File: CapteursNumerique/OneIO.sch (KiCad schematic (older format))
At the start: 5 parts, among them J14 Conn IO, J15 DIS LED

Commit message: Capteurs num production
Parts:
- D8: LCSC Part (none) -> C74346
- J14: JLCPCB BOM (none) -> 0
- J15: footprint Jumper:SolderJumper-2_P1.3mm_Bridged2Bar_Pad1.0x1.5mm -> Jumper:SolderJumper-2_P1.3mm_Open_Pad1.0x1.5mm; JLCPCB BOM (none) -> 0
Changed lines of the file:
@@
 $Descr A4 11693 8268
 encoding utf-8
-Sheet 4 9
+Sheet 9 9
 Title ""
 Date ""
@@
 AR Path="/5FC99C55/5FC6EE3F" Ref="#PWR010"  Part="1"
 AR Path="/5FC9F45B/5FC6EE3F" Ref="#PWR016"  Part="1"
-F 0 "#PWR06" H 5620 3000 50  0001 C CNN
+F 0 "#PWR016" H 5620 3000 50  0001 C CNN
 F 1 "+5V" H 5635 3323 50  0000 C CNN
 F 2 "" H 5620 3150 50  0001 C CNN
@@
 AR Path="/5FC99C55/5FC6F675" Ref="R14"  Part="1"
 AR Path="/5FC9F45B/5FC6F675" Ref="R20"  Part="1"
-F 0 "R10" H 5688 4076 50  0000 L CNN
+F 0 "R20" H 5688 4076 50  0000 L CNN
 F 1 "10k" H 5688 3985 50  0000 L CNN
 F 2 "Resistor_SMD:R_0805_2012Metric_Pad1.20x1.40mm_HandSolder" V 5660 4020 50  0001 C CNN
@@
 AR Path="/5FC99C55/5FC71F08" Ref="R15"  Part="1"
 AR Path="/5FC9F45B/5FC71F08" Ref="R21"  Part="1"
-F 0 "R11" H 6068 4076 50  0000 L CNN
+F 0 "R21" H 6068 4076 50  0000 L CNN
 F 1 "150" H 6068 3985 50  0000 L CNN
 F 2 "Resistor_SMD:R_0805_2012Metric_Pad1.20x1.40mm_HandSolder" V 6040 4020 50  0001 C CNN
@@
 AR Path="/5FC99C55/5FC72465" Ref="D6"  Part="1"
 AR Path="/5FC9F45B/5FC72465" Ref="D9"  Part="1"
-F 0 "D4" V 6039 4242 50  0000 R CNN
+F 0 "D9" V 6039 4242 50  0000 R CNN
 F 1 "YELLOW" V 5948 4242 50  0000 R CNN
 F 2 "LED_SMD:LED_0805_2012Metric_Pad1.15x1.40mm_HandSolder" H 6000 4360 50  0001 C CNN
 F 3 "~" H 6000 4360 50  0001 C CNN
+F 4 "C74346" V 6000 4360 50  0001 C CNN "LCSC Part"
 	1    6000 4360
 	0    -1   -1   0
@@
 AR Path="/5FC99C55/5FC77683" Ref="J11"  Part="1"
 AR Path="/5FC9F45B/5FC77683" Ref="J17"  Part="1"
-F 0 "J7" V 6004 3580 50  0000 L CNN
+F 0 "J17" V 6004 3580 50  0000 L CNN
 F 1 "DIS LED" V 6095 3580 50  0000 L CNN
-F 2 "Jumper:SolderJumper-2_P1.3mm_Bridged2Bar_Pad1.0x1.5mm" H 6000 3500 50  0001 C CNN
+F 2 "Jumper:SolderJumper-2_P1.3mm_Open_Pad1.0x1.5mm" H 6000 3500 50  0001 C CNN
 F 3 "~" H 6000 3500 50  0001 C CNN
+F 4 "0" V 6000 3500 50  0001 C CNN "JLCPCB BOM"
 	1    6000 3500
 	0    1    1    0
@@
 AR Path="/5FC99C55/5FC7B130" Ref="#PWR09"  Part="1"
 AR Path="/5FC9F45B/5FC7B130" Ref="#PWR015"  Part="1"
-F 0 "#PWR05" H 5370 4760 50  0001 C CNN
+F 0 "#PWR015" H 5370 4760 50  0001 C CNN
 F 1 "GND" H 5375 4837 50  0000 C CNN
 F 2 "" H 5370 5010 50  0001 C CNN
@@
 AR Path="/5FC99C55/5FC7CA9C" Ref="J10"  Part="1"
 AR Path="/5FC9F45B/5FC7CA9C" Ref="J16"  Part="1"
-F 0 "J6" H 4938 4505 50  0000 C CNN
+F 0 "J16" H 4938 4505 50  0000 C CNN
 F 1 "Conn IO" H 4938 4596 50  0000 C CNN
 F 2 "Connector_PinHeader_2.54mm:PinHeader_1x03_P2.54mm_Vertical" H 5020 4830 50  0001 C CNN
 F 3 "~" H 5020 4830 50  0001 C CNN
+F 4 "0" H 5020 4830 50  0001 C CNN "JLCPCB BOM"
 	1    5020 4830
 	-1   0    0    1

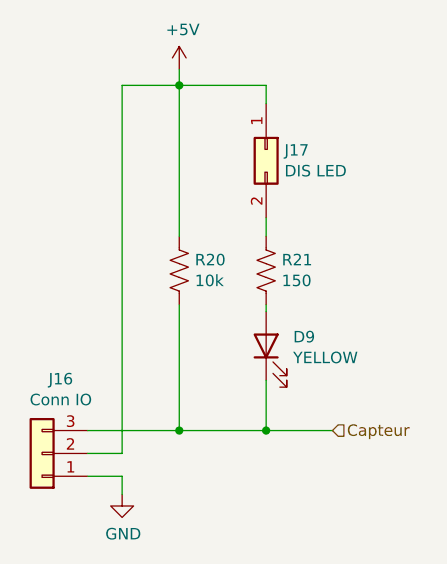
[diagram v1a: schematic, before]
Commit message: Module alim ISO, clean master alim
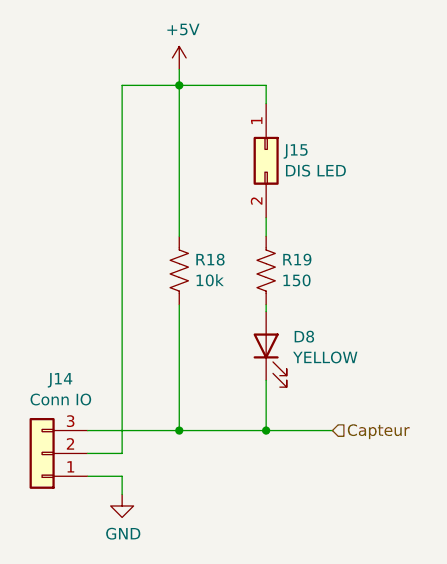
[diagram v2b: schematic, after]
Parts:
- R18: LCSC Part (none) -> C17414
- R19: LCSC Part (none) -> C17471
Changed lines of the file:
@@
 $Descr A4 11693 8268
 encoding utf-8
-Sheet 9 9
+Sheet 8 9
 Title ""
 Date ""
@@
 AR Path="/5FC99C55/5FC6EE3F" Ref="#PWR010"  Part="1"
 AR Path="/5FC9F45B/5FC6EE3F" Ref="#PWR016"  Part="1"
-F 0 "#PWR016" H 5620 3000 50  0001 C CNN
+F 0 "#PWR014" H 5620 3000 50  0001 C CNN
 F 1 "+5V" H 5635 3323 50  0000 C CNN
 F 2 "" H 5620 3150 50  0001 C CNN
@@
 AR Path="/5FC99C55/5FC6F675" Ref="R14"  Part="1"
 AR Path="/5FC9F45B/5FC6F675" Ref="R20"  Part="1"
-F 0 "R20" H 5688 4076 50  0000 L CNN
+F 0 "R18" H 5688 4076 50  0000 L CNN
 F 1 "10k" H 5688 3985 50  0000 L CNN
 F 2 "Resistor_SMD:R_0805_2012Metric_Pad1.20x1.40mm_HandSolder" V 5660 4020 50  0001 C CNN
 F 3 "~" H 5620 4030 50  0001 C CNN
+F 4 "C17414" H 5620 4030 50  0001 C CNN "LCSC Part"
 	1    5620 4030
 	1    0    0    -1
@@
 AR Path="/5FC99C55/5FC71F08" Ref="R15"  Part="1"
 AR Path="/5FC9F45B/5FC71F08" Ref="R21"  Part="1"
-F 0 "R21" H 6068 4076 50  0000 L CNN
+F 0 "R19" H 6068 4076 50  0000 L CNN
 F 1 "150" H 6068 3985 50  0000 L CNN
 F 2 "Resistor_SMD:R_0805_2012Metric_Pad1.20x1.40mm_HandSolder" V 6040 4020 50  0001 C CNN
 F 3 "~" H 6000 4030 50  0001 C CNN
+F 4 "C17471" H 6000 4030 50  0001 C CNN "LCSC Part"
 	1    6000 4030
 	1    0    0    -1
@@
 AR Path="/5FC99C55/5FC72465" Ref="D6"  Part="1"
 AR Path="/5FC9F45B/5FC72465" Ref="D9"  Part="1"
-F 0 "D9" V 6039 4242 50  0000 R CNN
+F 0 "D8" V 6039 4242 50  0000 R CNN
 F 1 "YELLOW" V 5948 4242 50  0000 R CNN
 F 2 "LED_SMD:LED_0805_2012Metric_Pad1.15x1.40mm_HandSolder" H 6000 4360 50  0001 C CNN
@@
 AR Path="/5FC99C55/5FC77683" Ref="J11"  Part="1"
 AR Path="/5FC9F45B/5FC77683" Ref="J17"  Part="1"
-F 0 "J17" V 6004 3580 50  0000 L CNN
+F 0 "J15" V 6004 3580 50  0000 L CNN
 F 1 "DIS LED" V 6095 3580 50  0000 L CNN
 F 2 "Jumper:SolderJumper-2_P1.3mm_Open_Pad1.0x1.5mm" H 6000 3500 50  0001 C CNN
@@
 AR Path="/5FC99C55/5FC7B130" Ref="#PWR09"  Part="1"
 AR Path="/5FC9F45B/5FC7B130" Ref="#PWR015"  Part="1"
-F 0 "#PWR015" H 5370 4760 50  0001 C CNN
+F 0 "#PWR013" H 5370 4760 50  0001 C CNN
 F 1 "GND" H 5375 4837 50  0000 C CNN
 F 2 "" H 5370 5010 50  0001 C CNN
@@
 AR Path="/5FC99C55/5FC7CA9C" Ref="J10"  Part="1"
 AR Path="/5FC9F45B/5FC7CA9C" Ref="J16"  Part="1"
-F 0 "J16" H 4938 4505 50  0000 C CNN
+F 0 "J14" H 4938 4505 50  0000 C CNN
 F 1 "Conn IO" H 4938 4596 50  0000 C CNN
 F 2 "Connector_PinHeader_2.54mm:PinHeader_1x03_P2.54mm_Vertical" H 5020 4830 50  0001 C CNN
